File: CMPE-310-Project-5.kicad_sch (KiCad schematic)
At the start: 3 parts, among them U4 8086_Min_Mode

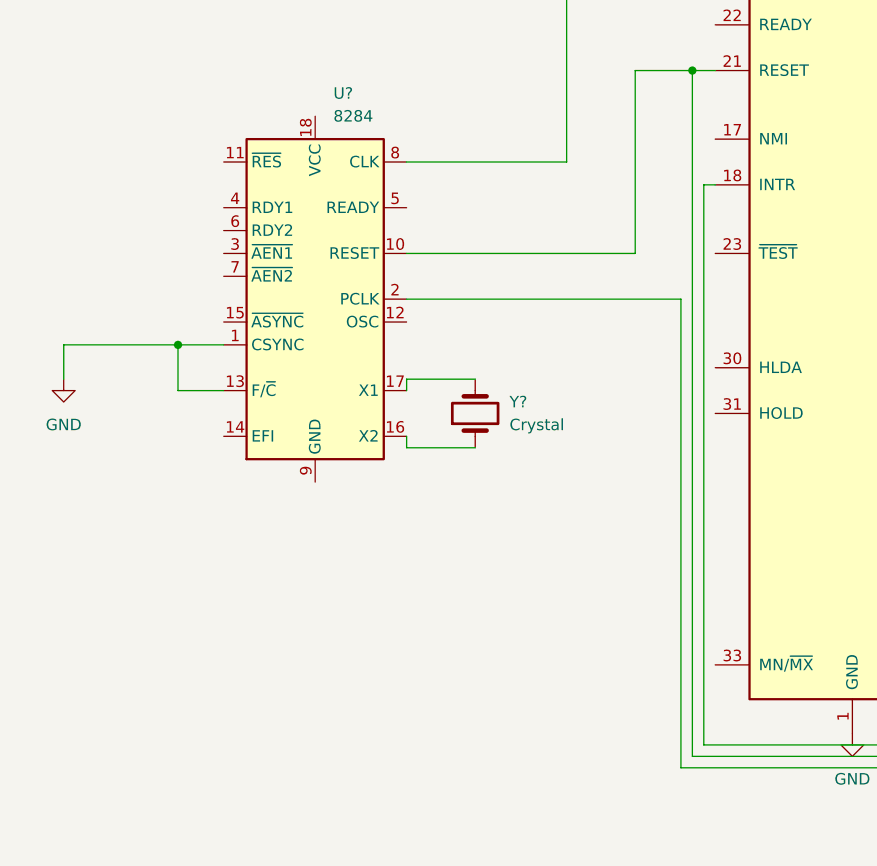
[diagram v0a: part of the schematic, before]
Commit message: Made reset switch for 8284
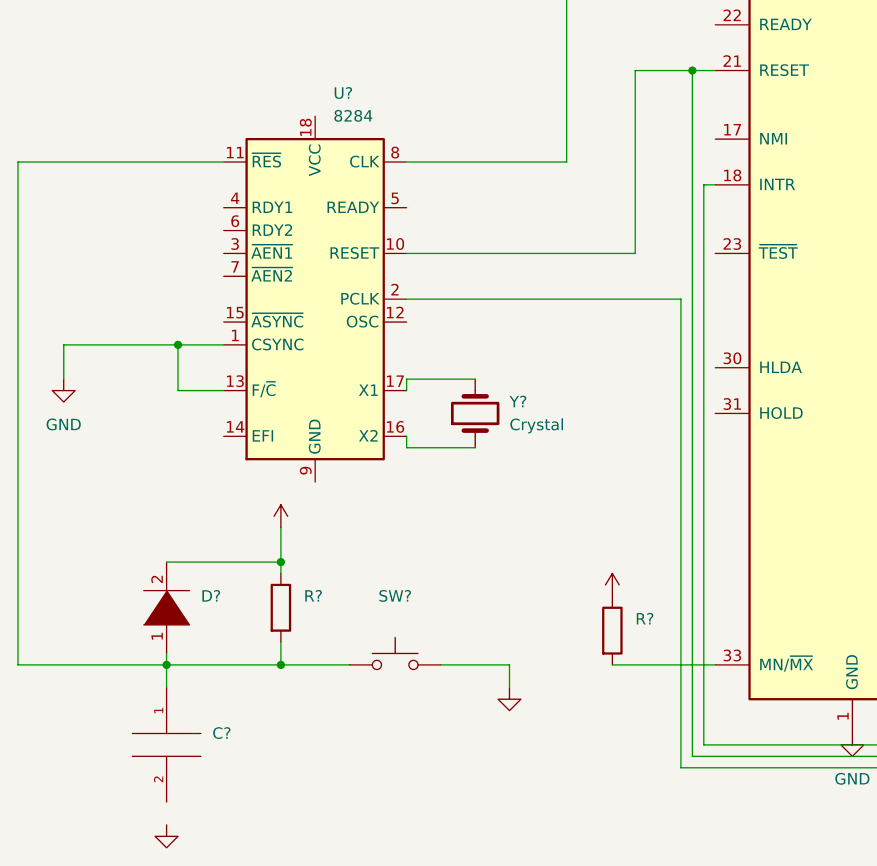
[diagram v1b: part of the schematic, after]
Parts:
- added C?: (no value), symbol pspice:C
- added D?: (no value), symbol pspice:DIODE
- added R? (x2): (no value), symbol Device:R
- added SW?: (no value), symbol Switch:SW_Push
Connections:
- net GND: now also SW?.2
- net at U?.11 (~{RES}): now also C?.1, D?.1 (K), R?.2, SW?.1
- net at U4.33 (MN/~{MX}): now also R?.2
- new net +5V: D?.2 (A), R?.1, R?.1

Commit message: Redid Bus
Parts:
- C?: value (none) -> C
- D?: value (none) -> DIODE
- R?: value (none) -> 10k
- R?: value (none) -> R
- SW?: value (none) -> SW_Push
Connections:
- net GND: now also R?.2, U4.33 (MN/~{MX})
- net Bus_wires/ALE: now reaches U4.25 (ALE)
- net Bus_wires/DEN: now reaches U4.26 (~{DEN})
- net Bus_wires/DT/R: now reaches U4.27 (DT/~{R})
- net Bus_wires/BHE/S7: now reaches U4.34 (~{BHE}/S7)
- net A0 renamed Bus_wires/AD0
- net A1 renamed Bus_wires/AD1
- net A10 renamed Bus_wires/AD10
- net A11 renamed Bus_wires/AD11
- net A12 renamed Bus_wires/AD12
- net A13 renamed Bus_wires/AD13
- net A14 renamed Bus_wires/AD14
- net A15 renamed Bus_wires/AD15
- net A16 renamed Bus_wires/A16/S3
- net A17 renamed Bus_wires/A17/S4
- net A18 renamed Bus_wires/A18/S5
- net A19 renamed Bus_wires/A19/S6
- net A2 renamed Bus_wires/AD2
- net A3 renamed Bus_wires/AD3
- net A4 renamed Bus_wires/AD4
- net A5 renamed Bus_wires/AD5
- net A6 renamed Bus_wires/AD6
- net A7 renamed Bus_wires/AD7
- net A8 renamed Bus_wires/AD8
- net A9 renamed Bus_wires/AD9
- net M/IO renamed Bus_wires/M/IO
- net RD renamed Bus_wires/RD
- net WR renamed Bus_wires/WR
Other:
- added sheet Bus_wires (Bus_sch.kicad_sch)
- sheet 8255_wires ports: added ControlBus; removed M/IO, RD, WR
- sheet CMOS_wires ports: added none; removed Data Bus, MRDC, MWTC, M/IO
- sheet INTR_wires ports: added none; removed M/IO, RD, WR
- moved on the sheet: R?, U4, Y?

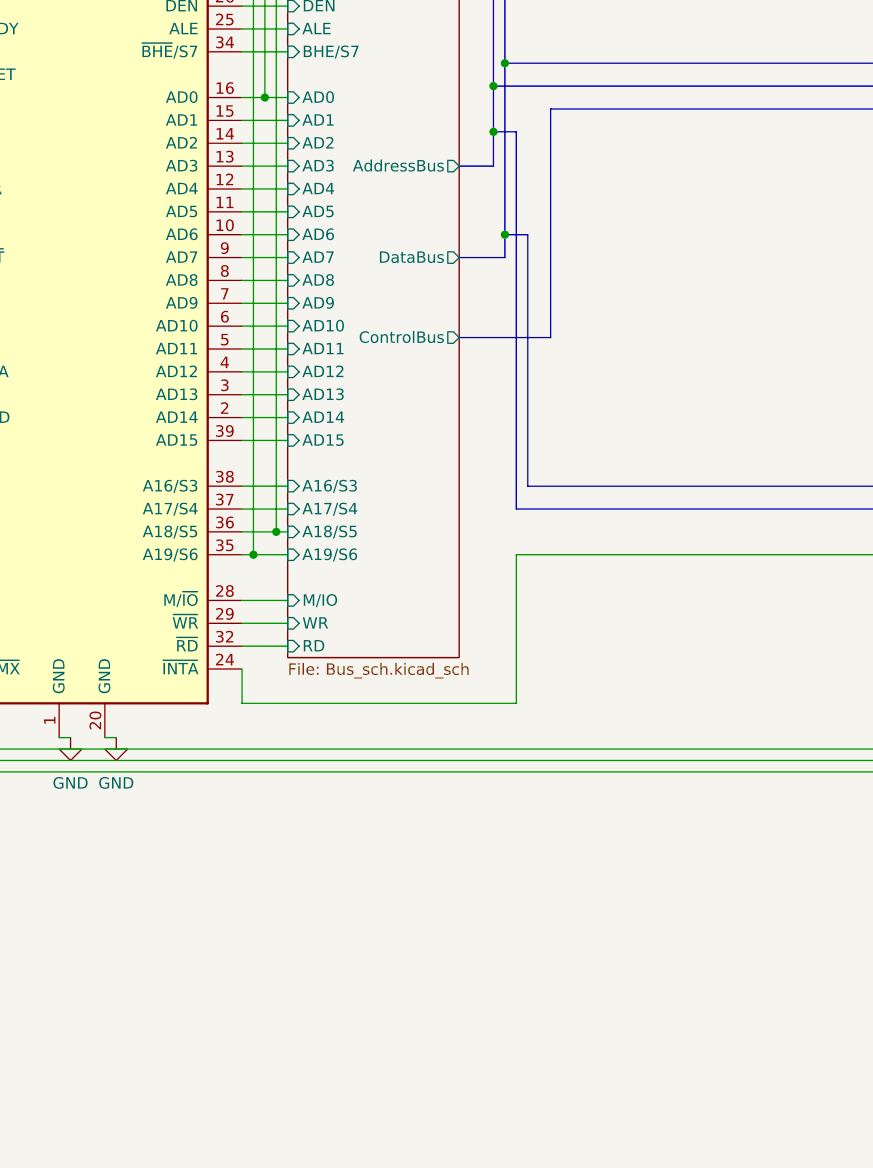
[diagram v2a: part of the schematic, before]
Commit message: Added headers to the necessary pins, and created IO device sheet
Added headers for the three chips and for the busses. Also created and started to address  decode the actual IO components.
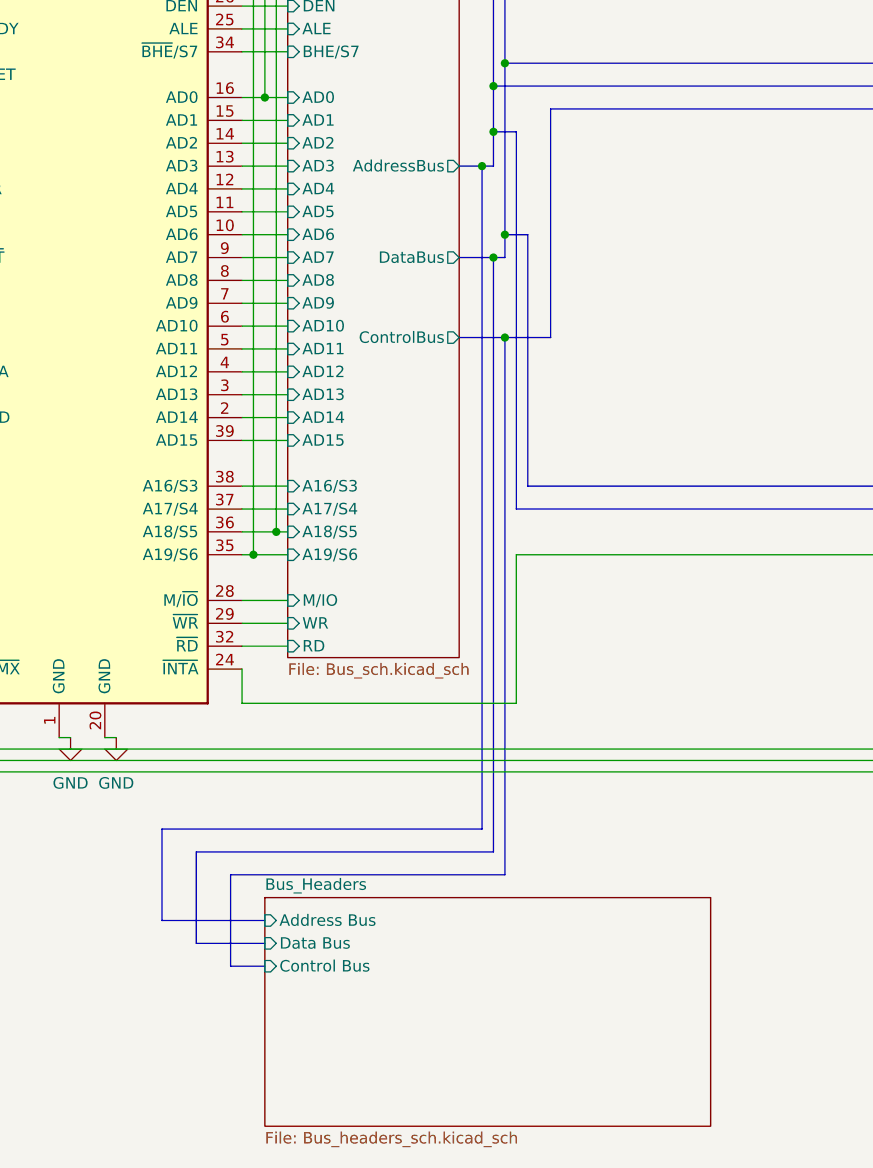
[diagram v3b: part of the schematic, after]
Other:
- added sheet Bus_Headers (Bus_headers_sch.kicad_sch)

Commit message: Moved Bus headers
Moved the bus headers to the sheet with the decoding to save space
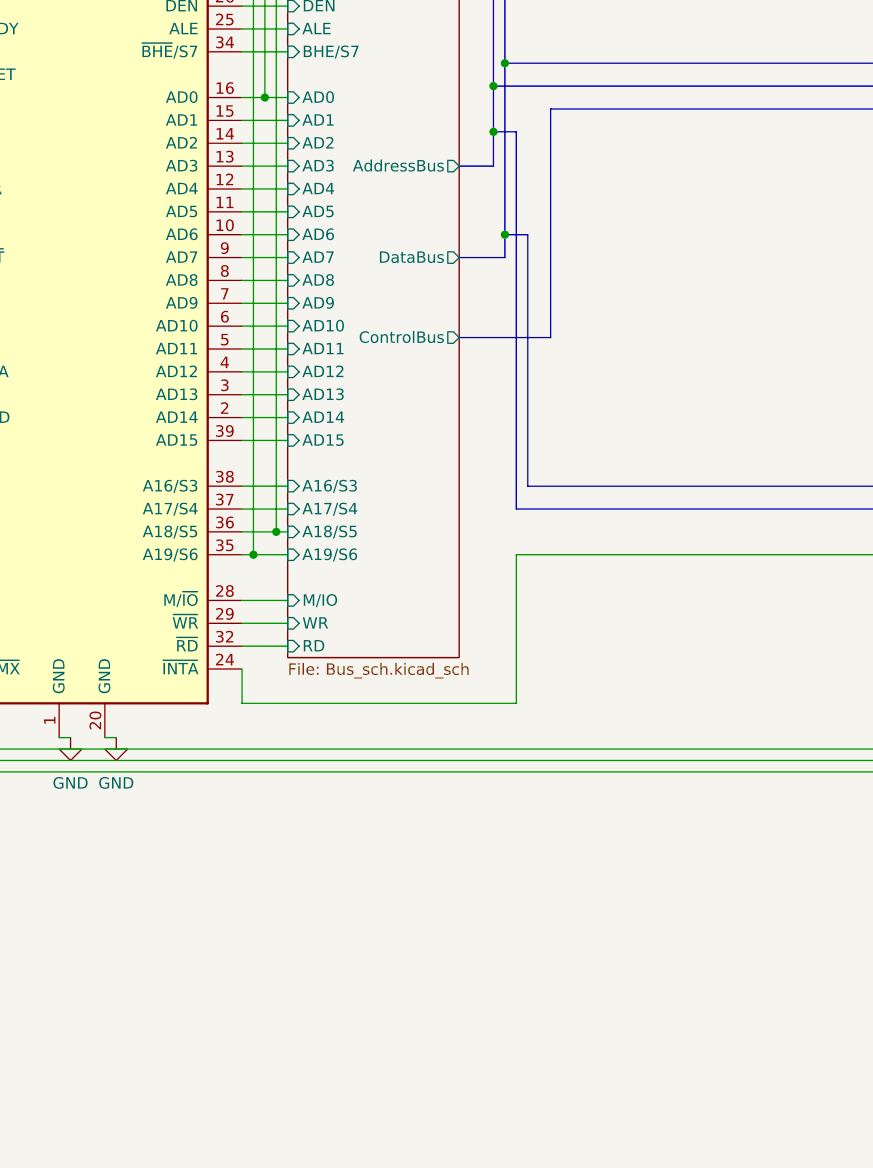
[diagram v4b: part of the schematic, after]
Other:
- removed sheet Bus_Headers
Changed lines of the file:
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@@
   (junction (at 143.51 91.44) (diameter 0) (color 0 0 0 0)
   )
-  (junction (at 140.97 83.82) (diameter 0) (color 0 0 0 0)
-  )
   (junction (at 118.11 124.46) (diameter 0) (color 0 0 0 0)
   )
@@
   (junction (at 33.02 139.7) (diameter 0) (color 0 0 0 0)
   )
-  (junction (at 142.24 93.98) (diameter 0) (color 0 0 0 0)
-  )
   (junction (at 142.24 74.93) (diameter 0) (color 0 0 0 0)
   )
@@
   (junction (at 115.57 127) (diameter 0) (color 0 0 0 0)
   )
-  (junction (at 143.51 102.87) (diameter 0) (color 0 0 0 0)
-  )
   (junction (at 116.84 76.2) (diameter 0) (color 0 0 0 0)
   )
@@
     (stroke (width 0) (type default) (color 0 0 0 0))
   )
-  (bus (pts (xy 116.84 170.18) (xy 109.22 170.18))
-    (stroke (width 0) (type default) (color 0 0 0 0))
-  )
   (wire (pts (xy 217.17 137.16) (xy 218.44 137.16))
     (stroke (width 0) (type default) (color 0 0 0 0))
@@
     (stroke (width 0) (type default) (color 0 0 0 0))
   )
-  (bus (pts (xy 105.41 157.48) (xy 140.97 157.48))
-    (stroke (width 0) (type default) (color 0 0 0 0))
-  )
   (wire (pts (xy 59.69 93.98) (xy 71.12 93.98))
     (stroke (width 0) (type default) (color 0 0 0 0))
@@
     (stroke (width 0) (type default) (color 0 0 0 0))
   )
-  (bus (pts (xy 105.41 167.64) (xy 105.41 157.48))
-    (stroke (width 0) (type default) (color 0 0 0 0))
-  )
   (wire (pts (xy 74.93 73.66) (xy 74.93 149.86))
     (stroke (width 0) (type default) (color 0 0 0 0))
   )
-  (bus (pts (xy 113.03 172.72) (xy 113.03 162.56))
-    (stroke (width 0) (type default) (color 0 0 0 0))
-  )
   (wire (pts (xy 114.3 76.2) (xy 116.84 76.2))
     (stroke (width 0) (type default) (color 0 0 0 0))
@@
     (stroke (width 0) (type default) (color 0 0 0 0))
   )
-  (bus (pts (xy 138.43 102.87) (xy 143.51 102.87))
-    (stroke (width 0) (type default) (color 0 0 0 0))
-  )
   (wire (pts (xy 76.2 148.59) (xy 214.63 148.59))
     (stroke (width 0) (type default) (color 0 0 0 0))
   )
-  (bus (pts (xy 138.43 83.82) (xy 140.97 83.82))
+  (bus (pts (xy 138.43 83.82) (xy 142.24 83.82))
     (stroke (width 0) (type default) (color 0 0 0 0))
   )
@@
     (stroke (width 0) (type default) (color 0 0 0 0))
   )
-  (bus (pts (xy 143.51 162.56) (xy 143.51 102.87))
-    (stroke (width 0) (type default) (color 0 0 0 0))
-  )
   (wire (pts (xy 73.66 151.13) (xy 218.44 151.13))
     (stroke (width 0) (type default) (color 0 0 0 0))
@@
     (stroke (width 0) (type default) (color 0 0 0 0))
   )
-  (bus (pts (xy 142.24 160.02) (xy 142.24 93.98))
-    (stroke (width 0) (type default) (color 0 0 0 0))
-  )
   (wire (pts (xy 63.5 139.7) (xy 68.58 139.7))
     (stroke (width 0) (type default) (color 0 0 0 0))
@@
     (stroke (width 0) (type default) (color 0 0 0 0))
   )
-  (bus (pts (xy 140.97 83.82) (xy 142.24 83.82))
-    (stroke (width 0) (type default) (color 0 0 0 0))
-  )
   (wire (pts (xy 63.5 83.82) (xy 63.5 63.5))
     (stroke (width 0) (type default) (color 0 0 0 0))
@@
     (stroke (width 0) (type default) (color 0 0 0 0))
   )
-  (bus (pts (xy 142.24 93.98) (xy 143.51 93.98))
-    (stroke (width 0) (type default) (color 0 0 0 0))
-  )
-  (bus (pts (xy 116.84 167.64) (xy 105.41 167.64))
-    (stroke (width 0) (type default) (color 0 0 0 0))
-  )
   (wire (pts (xy 34.29 109.22) (xy 34.29 104.14))
     (stroke (width 0) (type default) (color 0 0 0 0))
@@
     (stroke (width 0) (type default) (color 0 0 0 0))
   )
-  (bus (pts (xy 109.22 160.02) (xy 142.24 160.02))
-    (stroke (width 0) (type default) (color 0 0 0 0))
-  )
   (wire (pts (xy 45.72 124.46) (xy 45.72 128.27))
     (stroke (width 0) (type default) (color 0 0 0 0))
@@
     (stroke (width 0) (type default) (color 0 0 0 0))
   )
-  (bus (pts (xy 116.84 172.72) (xy 113.03 172.72))
-    (stroke (width 0) (type default) (color 0 0 0 0))
-  )
   (wire (pts (xy 114.3 111.76) (xy 119.38 111.76))
     (stroke (width 0) (type default) (color 0 0 0 0))
@@
     (stroke (width 0) (type default) (color 0 0 0 0))
   )
-  (bus (pts (xy 109.22 170.18) (xy 109.22 160.02))
-    (stroke (width 0) (type default) (color 0 0 0 0))
-  )
   (wire (pts (xy 33.02 139.7) (xy 33.02 142.24))
     (stroke (width 0) (type default) (color 0 0 0 0))
@@
     (stroke (width 0) (type default) (color 0 0 0 0))
   )
-  (bus (pts (xy 113.03 162.56) (xy 143.51 162.56))
-    (stroke (width 0) (type default) (color 0 0 0 0))
-  )
   (wire (pts (xy 114.3 66.04) (xy 119.38 66.04))
     (stroke (width 0) (type default) (color 0 0 0 0))
@@
     (stroke (width 0) (type default) (color 0 0 0 0))
   )
-  (bus (pts (xy 143.51 102.87) (xy 148.59 102.87))
-    (stroke (width 0) (type default) (color 0 0 0 0))
-  )
-  (bus (pts (xy 140.97 157.48) (xy 140.97 83.82))
+  (bus (pts (xy 138.43 102.87) (xy 148.59 102.87))
     (stroke (width 0) (type default) (color 0 0 0 0))
   )
@@
     (stroke (width 0) (type default) (color 0 0 0 0))
   )
-  (bus (pts (xy 138.43 93.98) (xy 142.24 93.98))
+  (bus (pts (xy 138.43 93.98) (xy 143.51 93.98))
     (stroke (width 0) (type default) (color 0 0 0 0))
   )
@@
     (pin "9")
   )
-  (sheet (at 116.84 165.1) (size 49.53 25.4) (fields_autoplaced)
-    (stroke (width 0.1524) (type solid) (color 0 0 0 0))
-    (fill (color 0 0 0 0.0000))
-    (property "Sheet name" "Bus_Headers" (id 0) (at 116.84 164.3884 0)
-      (effects (font (size 1.27 1.27)) (justify left bottom))
-    )
-    (property "Sheet file" "Bus_headers_sch.kicad_sch" (id 1) (at 116.84 191.0846 0)
-      (effects (font (size 1.27 1.27)) (justify left top))
-    )
-    (pin "Control Bus" input (at 116.84 172.72 180)
-      (effects (font (size 1.27 1.27)) (justify left))
-    )
-    (pin "Data Bus" input (at 116.84 170.18 180)
-      (effects (font (size 1.27 1.27)) (justify left))
-    )
-    (pin "Address Bus" input (at 116.84 167.64 180)
-      (effects (font (size 1.27 1.27)) (justify left))
-    )
-  )
   (sheet (at 222.25 69.85) (size 58.42 34.29) (fields_autoplaced)
     (stroke (width 0.1524) (type solid) (color 0 0 0 0))
@@
     (path "/87af81b5-cad9-406d-8283-65af2b602860/ed705d0b-56ef-479c-b140-27b7dd746870" (page "5"))
     (path "/e28c63c9-ea84-495f-a09f-7c14469ef64f" (page "6"))
-    (path "/5fc3593e-b9e8-49bd-9166-3ed0c5e60597" (page "7"))
     (path "/87af81b5-cad9-406d-8283-65af2b602860/ccdbd1e9-f638-4a0b-8283-b27a59eb17a3" (page "8"))
   )
@@
       (reference "DS?") (unit 1) (value "LCD4x20") (footprint "LCD4x20")
     )
-    (path "/5fc3593e-b9e8-49bd-9166-3ed0c5e60597/06070a0d-cffc-4dd6-849e-c038b4f5aeca"
-      (reference "J?") (unit 1) (value "Conn_01x20_Male") (footprint "")
-    )
     (path "/87af81b5-cad9-406d-8283-65af2b602860/269af414-30c7-41dc-8249-f1dd308917a2"
       (reference "J?") (unit 1) (value "Conn_01x02_Male") (footprint "")
@@
       (reference "J?") (unit 1) (value "DSUB-9") (footprint "DSUB-9")
     )
-    (path "/5fc3593e-b9e8-49bd-9166-3ed0c5e60597/49931089-1ce7-4471-a96f-74409a7e7cf1"
-      (reference "J?") (unit 1) (value "Conn_01x16_Male") (footprint "")
-    )
     (path "/65a0be0e-e533-4531-a6d7-d67f7f67ab34/5d4c0c42-e45a-426e-a48c-08086ef9d8b1"
       (reference "J?") (unit 1) (value "Conn_01x08_Male") (footprint "")
@@
       (reference "J?") (unit 1) (value "Conn_01x08_Male") (footprint "")
     )
+    (path "/e28c63c9-ea84-495f-a09f-7c14469ef64f/788aa65c-d886-48bc-b0a3-d0cf3a81ea92"
+      (reference "J?") (unit 1) (value "Conn_01x16_Male") (footprint "")
+    )
     (path "/65a0be0e-e533-4531-a6d7-d67f7f67ab34/ac92cbd3-c396-45d8-b4e2-c983091dec7e"
       (reference "J?") (unit 1) (value "Conn_01x08_Male") (footprint "")
     )
+    (path "/e28c63c9-ea84-495f-a09f-7c14469ef64f/b1f28974-c9e8-42e7-b670-1d34b4edf577"
+      (reference "J?") (unit 1) (value "Conn_01x20_Male") (footprint "")
+    )
     (path "/87af81b5-cad9-406d-8283-65af2b602860/b3e35886-6be2-45d7-954e-678128887b3c"
       (reference "J?") (unit 1) (value "Conn_01x03_Male") (footprint "")
@@
       (reference "J?") (unit 1) (value "Conn_01x08_Male") (footprint "")
     )
+    (path "/e28c63c9-ea84-495f-a09f-7c14469ef64f/d915edaa-c751-4eac-80da-425a0ab654dd"
+      (reference "J?") (unit 1) (value "Conn_01x03_Male") (footprint "")
+    )
     (path "/65a0be0e-e533-4531-a6d7-d67f7f67ab34/f0c5269a-b5d4-4bc1-98fb-8c65af9bfb55"
       (reference "J?") (unit 1) (value "Conn_01x08_Male") (footprint "")
@@
       (reference "J?") (unit 1) (value "Conn_01x08_Male") (footprint "")
     )
-    (path "/5fc3593e-b9e8-49bd-9166-3ed0c5e60597/fc2e57ee-a740-4d20-afb5-e2779370f6d2"
-      (reference "J?") (unit 1) (value "Conn_01x03_Male") (footprint "")
-    )
     (path "/87af81b5-cad9-406d-8283-65af2b602860/fea5533d-abef-41be-a549-2822bf2ac716"
